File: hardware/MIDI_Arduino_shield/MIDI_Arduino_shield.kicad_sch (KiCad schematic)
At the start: 32 parts, among them J2 MIDI OUT, J3 MIDI IN, J4 I2C, Q1 2N3904, SW1 RotaryEncoder_Switch, SW2 SW_Push, SW3 SW_Push, SW4 SW_DPDT_x2, U2 6N139

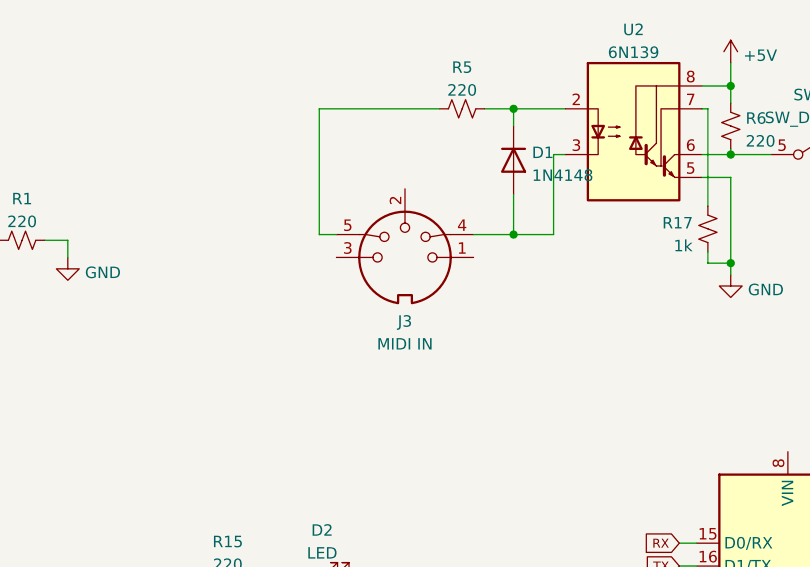
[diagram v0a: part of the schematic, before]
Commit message: Fixed MIDI pinout swap
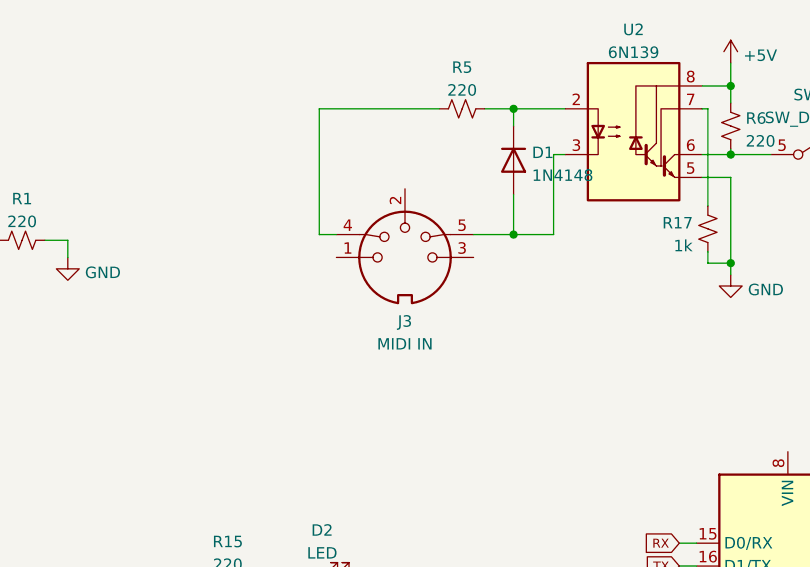
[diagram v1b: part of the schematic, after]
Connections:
- net at R5.1: now also J3.4; no longer J3.5
- net at D1.2 (A), U2.3 (C2): now also J3.5; no longer J3.4
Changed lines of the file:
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@@
     (pin "S2")
   )
-  (symbol (lib_id "Connector:DIN-5_180degree") (at 172.72 61.595 0) (mirror y) (unit 1)
+  (symbol (lib_id "Connector:DIN-5_180degree") (at 172.72 61.595 0) (unit 1)
     (in_bom yes) (on_board yes) (fields_autoplaced)
-    (property "Reference" "J3" (id 0) (at 172.7199 68.7054 0))
-    (property "Value" "MIDI IN" (id 1) (at 172.7199 71.2423 0))
+    (property "Reference" "J3" (id 0) (at 172.7201 68.7054 0))
+    (property "Value" "MIDI IN" (id 1) (at 172.7201 71.2423 0))
     (property "Footprint" "w_conn_av:din-5" (id 2) (at 172.72 61.595 0)
       (effects (font (size 1.27 1.27)) hide)
